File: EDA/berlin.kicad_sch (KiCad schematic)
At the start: 250 parts, among them SW105-? MXSwitch, SW124-? MXSwitch, SW20-? MXSwitch, SW39-? MXSwitch, SW4-? MXSwitch, SW5-? MXSwitch, SW6-? MXSwitch, SW64-? MXSwitch, SW78-? MXSwitch, SW88-? MXSwitch, SW90-? MXSwitch

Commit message: clean up the key matrix
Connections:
- net Col10: now also SW?.1 (Col); no longer SW64-?.1 (Col)
- net Col11: now also SW78-?.1 (Col); no longer SW64-?.1 (Col)
- net Col12: now also SW88-?.1 (Col); no longer SW?.1 (Col)
- net Col13: now also SW90-?.1 (Col); no longer SW78-?.1 (Col)
- net Col14: now also SW?.1 (Col), SW?.1 (Col), SW?.1 (Col), SW?.1 (Col), SW?.1 (Col)
- net Col15: now also SW?.1 (Col), SW?.1 (Col), SW?.1 (Col), SW?.1 (Col), SW?.1 (Col), SW?.1 (Col)
- net Col16: now also SW?.1 (Col), SW?.1 (Col), SW?.1 (Col), SW?.1 (Col), SW?.1 (Col), SW?.S1
- net Col17: now also SW105-?.1 (Col), SW?.1 (Col), SW?.1 (Col), SW?.1 (Col), SW?.1 (Col), SW?.1 (Col)
- net Col18: now also SW124-?.1 (Col), SW?.1 (Col), SW?.1 (Col), SW?.1 (Col), SW?.1 (Col)
- net Col19: now also SW?.1 (Col), SW?.1 (Col), SW?.1 (Col), SW?.1 (Col), SW?.1 (Col), SW?.1 (Col)
- net Col8: now also SW64-?.1 (Col)
- net Col9: now also SW64-?.1 (Col)
- net Row1: now also D?.1 (K), D?.1 (K), D?.1 (K)
- net Row2: now also D?.1 (K), D?.1 (K), D?.1 (K), D?.1 (K), D?.1 (K), D?.1 (K)
- net Row3: now also D?.1 (K), D?.1 (K), D?.1 (K), D?.1 (K), D?.1 (K); no longer D?.1 (K)
- net Row4: now also D?.1 (K), D?.1 (K), D?.1 (K), D?.1 (K), D?.1 (K), D?.1 (K)
- net Row5: now also D?.1 (K), D?.1 (K), D?.1 (K), D?.1 (K), D?.1 (K), D?.1 (K); no longer D?.1 (K)
- net Row6: now also D?.1 (K), D?.1 (K), D?.1 (K), D?.1 (K)
- net Row7: now also D?.1 (K), D?.1 (K), D?.1 (K), D?.1 (K), D?.1 (K), D?.1 (K), D?.1 (K)
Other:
- note added: "#"
- note added: ","
- note added: "<>"
- note added: "Backspace"
- note added: "Backtick"
- note added: "P16"
- note added: "P17"
- note added: "Ä"
- note added: "Ö"
- note added: "Ü"
- note added: "ß"
- note removed: "' ""
- note removed: ", <"
- note removed: "- _"
- note removed: ". >"
- note removed: "/ ?"
- note removed: "; :"
- note removed: "= +"
- note removed: "BackSpace"
- note removed: "ISO Enter"
- note removed: "ISO \ |"
- note removed: "ISO `~{}"
- note removed: "[{"
- note removed: "]}"
- moved on the sheet: D?, L?, SW105-?, SW124-?, SW64-?, SW78-?, SW88-?, SW90-?, SW?

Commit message: blursed schematic
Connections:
- net Col12: now also SW?.1 (Col); no longer SW88-?.1 (Col)
- net Col13: now also SW88-?.1 (Col); no longer SW?.1 (Col)
- net Row4: now also D?.1 (K); no longer D?.1 (K), D?.1 (K)
- net Row5: now also D?.1 (K), D?.1 (K); no longer D?.1 (K), D?.1 (K)
- net Row6: now also D?.1 (K), D?.1 (K), D?.1 (K); no longer D?.1 (K), D?.1 (K)
- net Row7: now also D?.1 (K), D?.1 (K), D?.1 (K); no longer D?.1 (K), D?.1 (K)
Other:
- note added: "' ""
- note added: ", <"
- note added: "- _"
- note added: ". >"
- note added: "/ ?"
- note added: "; :"
- note added: "= +"
- note added: "BackSpace"
- note added: "ISO Enter"
- note added: "ISO \ |"
- note added: "ISO `~{}"
- note added: "[{"
- note added: "]}"
- note added: "back"
- note added: "friday13"
- note added: "play"
- note added: "pmslps4"
- note added: "skip"
- note removed: "#"
- note removed: ","
- note removed: "<>"
- note removed: "Backspace"
- note removed: "Backtick"
- note removed: "P13"
- note removed: "P14"
- note removed: "P15"
- note removed: "P16"
- note removed: "P17"
- note removed: "Ä"
- note removed: "Ö"
- note removed: "Ü"
- note removed: "ß"
- moved on the sheet: D?, L?, SW105-?, SW124-?, SW20-?, SW39-?, SW4-?, SW5-?, SW6-?, SW64-?, SW78-?, SW88-?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

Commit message: added additional schematics
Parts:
- added C? (x16): 10u, Capacitor_SMD:C_1206_3216Metric_Pad1.42x1.75mm_HandSolder, symbol Device:C
- added C? (x16): 100nF, Capacitor_SMD:C_0805_2012Metric_Pad1.15x1.40mm_HandSolder, symbol Device:C
- added C? (x6): 22uF, Capacitor_SMD:C_1206_3216Metric_Pad1.42x1.75mm_HandSolder, symbol Device:C
- added C? (x7): 100n, Capacitor_SMD:C_0805_2012Metric_Pad1.15x1.40mm_HandSolder, symbol Device:C
- added C?: 4.7n, Capacitor_SMD:C_0805_2012Metric_Pad1.15x1.40mm_HandSolder, symbol Device:C
- added D?: RB060M-60TR, acheronComponents:D_SOD-123, symbol Device:D_Schottky_Small
- added D?: 1N4148, acheronComponents:D_SOD-123, symbol Diode:1N4148
- added F?: 1.5A Polyfuse, Fuse:Fuse_1812_4532Metric_Pad1.30x3.40mm_HandSolder, symbol Device:Polyfuse
- added H?: MountingHole_Pad, MountingHole:MountingHole_3.5mm_Pad_Via, symbol Mechanical:MountingHole_Pad
- added HA? (x4): MountingHole, acheronMountingHoles:ToolingHole_1.152mm_(for_JLCPCB_SMT), symbol Mechanical:MountingHole
- added J?: TYPE-C-31-M12_13, acheronConnectors:TYPE-C-31-M-12, symbol Boston-controller-STM32-rescue:TYPE-C-31-M12_13-Acheron
- added J?: Conn_ARM_JTAG_SWD_10, Connector_PinSocket_2.54mm:PinSocket_2x05_P2.54mm_Vertical, symbol acheronSymbols:Conn_ARM_JTAG_SWD_10
- added L? (x2): L_Core_Ferrite, Inductor_SMD:L_0805_2012Metric_Pad1.15x1.40mm_HandSolder, symbol Device:L_Core_Ferrite
- added L?: 6.8uH, SumidaInductor:Sumida0624CDMCC, symbol Device:L
- added LED? (x143): LED, LED_THT:LED_D3.0mm_Clear, symbol Device:LED
- added LED?: NeoPixel_THT, LED_THT:LED_D5.0mm-4_RGB, symbol LED:NeoPixel_THT
- added LOGO?: Logo_Open_Hardware_Large, Symbol:OSHW-Logo_11.4x12mm_SilkScreen, symbol Graphic:Logo_Open_Hardware_Large
- added Q?: DTC123J, Package_TO_SOT_SMD:SOT-23, symbol Transistor_BJT:DTC123J
- added Q?: AO4406AL, acheronComponents:SOIC-8, symbol Boston-controller-STM32-rescue:AO4406AL-Acheron
- added R? (x136): 100 1%, Resistor_SMD:R_0805_2012Metric_Pad1.15x1.40mm_HandSolder, symbol Device:R
- added R? (x2): 5.1k, Resistor_SMD:R_0805_2012Metric_Pad1.15x1.40mm_HandSolder, symbol Device:R
- added R?: 100k, Resistor_SMD:R_0805_2012Metric_Pad1.15x1.40mm_HandSolder, symbol Device:R
- added R? (x3): 330, Resistor_THT:R_Axial_DIN0207_L6.3mm_D2.5mm_P7.62mm_Horizontal, symbol Device:R
- added R?: 1M 1%, Resistor_SMD:R_0805_2012Metric_Pad1.15x1.40mm_HandSolder, symbol Device:R
- added R?: 330k 1%, Resistor_SMD:R_0805_2012Metric_Pad1.15x1.40mm_HandSolder, symbol Device:R
- added R? (x3): 10k, Resistor_SMD:R_0805_2012Metric_Pad1.15x1.40mm_HandSolder, symbol Device:R
- added SW?: SW_Push, Button_Switch_THT:SW_PUSH_6mm_H5mm, symbol Switch:SW_Push
- added U?: SN74LVC1T45DCK, Package_TO_SOT_SMD:SOT-23-6_Handsoldering, symbol Logic_LevelTranslator:SN74LVC1T45DCK
- added U?: STM32F072CBTx, Package_QFP:LQFP-48_7x7mm_P0.5mm, symbol MCU_ST_STM32F0:STM32F072CBTx
- added U?: USBLC6-2SC6, Package_TO_SOT_SMD:SOT-23-6, symbol Power_Protection:USBLC6-2SC6
- added U?: AP63203WU-7, Package_TO_SOT_SMD:TSOT-23-6_HandSoldering, symbol Boston-controller-STM32-rescue:AP63203WU-7-Acheron
- added UA?: STM32F072CBUx, Package_DFN_QFN:QFN-48-1EP_7x7mm_P0.5mm_EP5.6x5.6mm, symbol MCU_ST_STM32F0:STM32F072CBUx
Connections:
- net Col1: now also U?.21 (PB10), UA?.21 (PB10)
- net Col10: now also U?.38 (PA15), UA?.38 (PA15)
- net Col11: now also U?.39 (PB3), UA?.39 (PB3)
- net Col12: now also U?.40 (PB4), UA?.40 (PB4)
- net Col13: now also U?.43 (PB7), UA?.43 (PB7)
- net Col14: now also U?.45 (PB8), UA?.45 (PB8)
- net Col15: now also U?.46 (PB9), UA?.46 (PB9)
- net Col16: now also U?.3 (PC14), UA?.3 (PC14)
- net Col17: now also U?.4 (PC15), UA?.4 (PC15)
- net Col18: now also U?.5 (PF0), UA?.5 (PF0)
- net Col19: now also U?.13 (PA3), UA?.13 (PA3)
- net Col2: now also U?.22 (PB11), UA?.22 (PB11)
- net Col3: now also U?.25 (PB12), UA?.25 (PB12)
- net Col4: now also U?.26 (PB13), UA?.26 (PB13)
- net Col5: now also U?.27 (PB14), UA?.27 (PB14)
- net Col6: now also U?.28 (PB15), UA?.28 (PB15)
- net Col7: now also U?.29 (PA8), UA?.29 (PA8)
- net Col8: now also U?.30 (PA9), UA?.30 (PA9)
- net Col9: now also U?.31 (PA10), UA?.31 (PA10)
- net EncA: now also R?.1, U?.2 (PC13), UA?.2 (PC13)
- net EncB: now also R?.1, U?.6 (PF1), UA?.6 (PF1)
- net GND: now also C?.2, C?.2, C?.2, C?.2, C?.2, C?.2, C?.2, C?.2, C?.2, C?.2, C?.2, C?.2, C?.2, C?.2, C?.2, C?.2, C?.2, D?.2 (A), J?.3 (GND), J?.5 (GND), J?.9 (GNDDetect), J?.A1 (GND), J?.B1 (GND), L?.1, L?.2, LED?.1 (K), LED?.1 (K), LED?.1 (K), LED?.2 (GND), Q?.1, Q?.2, Q?.2 (E), Q?.3, R?.1, R?.1, R?.1, R?.1, R?.1, U?.2 (GND), U?.2 (GND), U?.23 (VSS), U?.35 (VSS), U?.4 (GND), U?.47 (VSS), U?.8 (VSSA), UA?.23 (VSS), UA?.35 (VSS), UA?.47 (VSS), UA?.49 (VSS), UA?.8 (VSSA)
- net Row1: now also U?.41 (PB5), UA?.41 (PB5)
- net Row2: now also U?.42 (PB6), UA?.42 (PB6)
- net Row3: now also U?.17 (PA7), UA?.17 (PA7)
- net Row4: now also U?.18 (PB0), UA?.18 (PB0)
- net Row5: now also U?.19 (PB1), UA?.19 (PB1)
- net Row6: now also U?.20 (PB2), UA?.20 (PB2)
- net Row7: now also U?.14 (PA4), UA?.14 (PA4)
- new net: LED?.2 (A), R?.2 (x127)
- new net: LED?.2 (A), LED?.2 (A), LED?.2 (A), R?.2
- new net: LED?.2 (A), LED?.2 (A), R?.2 (x5)
- new net: R?.2, U?.4 (B)
- new net: J?.A5 (CC1), R?.2
- new net: J?.B5 (CC2), R?.2
- new net: J?.S (SHIELD), L?.1
- new net: R?.2, U?.12 (PA2), UA?.12 (PA2)
- new net: R?.2, U?.11 (PA1), UA?.11 (PA1)
- new net: R?.2, U?.10 (PA0), UA?.10 (PA0)
- new net: D?.1 (K), R?.2
- new net: D?.2 (A), Q?.1 (B), SW?.2
- new net: H?.1, L?.2
- new net: C?.2, L?.1, U?.5 (SW)
- new net: C?.1, U?.6 (BST)
- new net: Q?.4 (G), R?.2, R?.2
- new net: Q?.3 (C), R?.2
- new net +3V3: C?.1, C?.1, C?.1, C?.1, C?.1, C?.1, C?.1, C?.1, C?.1, C?.1, C?.1, C?.1, C?.1, C?.1, C?.1, C?.1, C?.1, C?.1, C?.1, C?.1, C?.1, C?.1, C?.1, C?.1, C?.1, C?.1, C?.1, C?.1, C?.1, C?.1, C?.1, C?.1, C?.1, C?.1, C?.1, C?.1, C?.1, C?.1, C?.1, J?.1 (VCC), L?.2, R?.1, R?.1, R?.1, R?.1, R?.1, R?.1, R?.1, R?.1, R?.1, R?.1, R?.1, R?.1, R?.1, R?.1, R?.1, R?.1, R?.1, R?.1, R?.1, R?.1, R?.1, R?.1, R?.1, R?.1, R?.1, R?.1, R?.1, R?.1, R?.1, R?.1, R?.1, R?.1, R?.1, R?.1, R?.1, R?.1, R?.1, R?.1, R?.1, R?.1, R?.1, R?.1, R?.1, R?.1, R?.1, R?.1, R?.1, R?.1, R?.1, R?.1, R?.1, R?.1, R?.1, R?.1, R?.1, R?.1, R?.1, R?.1, R?.1, R?.1, R?.1, R?.1, R?.1, R?.1, R?.1, R?.1, R?.1, R?.1, R?.1, R?.1, R?.1, R?.1, R?.1, R?.1, R?.1, R?.1, R?.1, R?.1, R?.1, R?.1, R?.1, R?.1, R?.1, R?.1, R?.1, R?.1, R?.1, R?.1, R?.1, R?.1, R?.1, R?.1, R?.1, R?.1, R?.1, R?.1, R?.1, R?.1, R?.1, R?.1, R?.1, R?.1, R?.1, R?.1, R?.1, R?.1, R?.1, R?.1, R?.1, R?.1, R?.1, R?.1, R?.1, R?.1, R?.1, R?.1, R?.1, R?.1, R?.1, R?.1, R?.1, R?.1, R?.1, R?.1, R?.1, R?.1, R?.1, R?.1, R?.1, R?.1, R?.1, R?.1, R?.1, R?.2, R?.2, SW?.1, U?.1 (FB), U?.1 (VBAT), U?.1 (VCCA), U?.24 (VDD), U?.36 (VDDIO2), U?.48 (VDD), U?.5 (DIR), U?.9 (VDDA), UA?.1 (VBAT), UA?.24 (VDD), UA?.36 (VDDIO2), UA?.48 (VDD), UA?.9 (VDDA)
- new net +5V: C?.1, C?.1, C?.1, D?.1 (K), F?.1, LED?.3 (VDD), R?.2, U?.2 (ENABLE), U?.3 (VIN), U?.6 (VCCB)
- new net BOOT0: C?.1, R?.1, R?.2, U?.44 (BOOT0), UA?.44 (BOOT0)
- new net CAP_INDICATOR: LED?.2 (A), R?.1
- new net D+: U?.33 (PA12), U?.4 (I/O2), UA?.33 (PA12)
- new net D-: U?.32 (PA11), U?.6 (I/O1), UA?.32 (PA11)
- new net DI: LED?.4 (DIN), R?.1
- new net Dbus+: J?.A6 (D+), J?.B6 (D+), U?.3 (I/O2)
- new net Dbus-: J?.A7 (D-), J?.B7 (D-), U?.1 (I/O1)
- new net LED_PWM: R?.1, U?.16 (PA6), UA?.16 (PA6)
- new net LED_switch: C?.2, C?.2, C?.2, C?.2, C?.2, C?.2, C?.2, C?.2, C?.2, C?.2, C?.2, C?.2, C?.2, C?.2, C?.2, C?.2, C?.2, C?.2, C?.2, C?.2, C?.2, C?.2, C?.2, C?.2, C?.2, C?.2, C?.2, C?.2, LED?.1 (K), LED?.1 (K), LED?.1 (K), LED?.1 (K), LED?.1 (K), LED?.1 (K), LED?.1 (K), LED?.1 (K), LED?.1 (K), LED?.1 (K), LED?.1 (K), LED?.1 (K), LED?.1 (K), LED?.1 (K), LED?.1 (K), LED?.1 (K), LED?.1 (K), LED?.1 (K), LED?.1 (K), LED?.1 (K), LED?.1 (K), LED?.1 (K), LED?.1 (K), LED?.1 (K), LED?.1 (K), LED?.1 (K), LED?.1 (K), LED?.1 (K), LED?.1 (K), LED?.1 (K), LED?.1 (K), LED?.1 (K), LED?.1 (K), LED?.1 (K), LED?.1 (K), LED?.1 (K), LED?.1 (K), LED?.1 (K), LED?.1 (K), LED?.1 (K), LED?.1 (K), LED?.1 (K), LED?.1 (K), LED?.1 (K), LED?.1 (K), LED?.1 (K), LED?.1 (K), LED?.1 (K), LED?.1 (K), LED?.1 (K), LED?.1 (K), LED?.1 (K), LED?.1 (K), LED?.1 (K), LED?.1 (K), LED?.1 (K), LED?.1 (K), LED?.1 (K), LED?.1 (K), LED?.1 (K), LED?.1 (K), LED?.1 (K), LED?.1 (K), LED?.1 (K), LED?.1 (K), LED?.1 (K), LED?.1 (K), LED?.1 (K), LED?.1 (K), LED?.1 (K), LED?.1 (K), LED?.1 (K), LED?.1 (K), LED?.1 (K), LED?.1 (K), LED?.1 (K), LED?.1 (K), LED?.1 (K), LED?.1 (K), LED?.1 (K), LED?.1 (K), LED?.1 (K), LED?.1 (K), LED?.1 (K), LED?.1 (K), LED?.1 (K), LED?.1 (K), LED?.1 (K), LED?.1 (K), LED?.1 (K), LED?.1 (K), LED?.1 (K), LED?.1 (K), LED?.1 (K), LED?.1 (K), LED?.1 (K), LED?.1 (K), LED?.1 (K), LED?.1 (K), LED?.1 (K), LED?.1 (K), LED?.1 (K), LED?.1 (K), LED?.1 (K), LED?.1 (K), LED?.1 (K), LED?.1 (K), LED?.1 (K), LED?.1 (K), LED?.1 (K), LED?.1 (K), LED?.1 (K), LED?.1 (K), LED?.1 (K), LED?.1 (K), LED?.1 (K), LED?.1 (K), LED?.1 (K), LED?.1 (K), LED?.1 (K), LED?.1 (K), LED?.1 (K), LED?.1 (K), LED?.1 (K), LED?.1 (K), LED?.1 (K), LED?.1 (K), LED?.1 (K), LED?.1 (K), LED?.1 (K), LED?.1 (K), LED?.1 (K), LED?.1 (K), LED?.1 (K), LED?.1 (K), LED?.1 (K), LED?.1 (K), LED?.1 (K), LED?.1 (K), LED?.1 (K), Q?.5 (D), Q?.6, Q?.7, Q?.8
- new net NRST: C?.1, J?.10 (~{RESET}), R?.1, U?.7 (NRST), UA?.7 (NRST)
- new net NUM_INDICATOR: LED?.2 (A), R?.1
- new net RGBLED: U?.15 (PA5), U?.3 (A), UA?.15 (PA5)
- new net SCRL_INDICATOR: LED?.2 (A), R?.1
- new net SWCLK: J?.4 (SWDCLK/TCK), U?.37 (PA14), UA?.37 (PA14)
- new net SWDIO: J?.2 (SWDIO/TMS), U?.34 (PA13), UA?.34 (PA13)
- new net VBUS: C?.1, F?.2, J?.A4 (VBUS), J?.B4 (VBUS), U?.5 (VBUS)
- no-connect marks 0 -> 4
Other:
- note added: "3.3V power"
- note added: "5mm through hole LED (3D-printed version only)"
- note added: "Backlight LEDs"
- note added: "Bulk caps"
- note added: "Bypass cap for the level shifter"
- note added: "Hole for grounding alu case"
- note added: "Holes for JLCPCB SMT tooling"
- note added: "ISP header"
- note added: "LED PWM MOSFET"
- note added: "LQFP-48"
- note added: "Level shifter"
- note added: "Lock LEDs"
- note added: "Logos, holes, misc."
- note added: "Microcontroller"
- note added: "Microprocessor Bypass caps"
- note added: "RGB LED stuff"
- note added: "Reset circuit"
- note added: "SMPS provides more LED current for backlight usage."
- note added: "Sumida 0624CDMCCDS-6R8MC"
- note added: "UFQFPN48 alternate"
- note added: "USB"
- note added: "USB ESD protection"

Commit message: update/fix switch descriptors
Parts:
- gave numbers to parts that had none: 123
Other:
- note added: ","
- note added: "ISO <> |"
- note added: "´"
- note added: "Ä"
- note added: "Ö"
- note added: "Ü"
- note added: "ß"
- note removed: "' ""
- note removed: ", <"
- note removed: "- _"
- note removed: ". >"
- note removed: "/ ?"
- note removed: "; :"
- note removed: "= +"
- note removed: "ISO \ |"
- note removed: "[{"
- note removed: "]}"

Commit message: tset
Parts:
- added R? (x3): 330, Resistor_THT:R_Axial_DIN0207_L6.3mm_D2.5mm_P7.62mm_Horizontal, symbol Device:R
- added R? (x2): 10k, Resistor_SMD:R_0805_2012Metric_Pad1.15x1.40mm_HandSolder, symbol Device:R
- added U?: STM32F072CBTx, Package_QFP:LQFP-48_7x7mm_P0.5mm, symbol MCU_ST_STM32F0:STM32F072CBTx
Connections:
- net +3V3: now also R?.2, R?.2, U?.1 (VBAT), U?.24 (VDD), U?.36 (VDDIO2), U?.48 (VDD), U?.9 (VDDA)
- net BOOT0: now also U?.44 (BOOT0)
- net CAP_INDICATOR: now also R?.1
- net Col1: now also U?.21 (PB10)
- net Col10: now also U?.38 (PA15)
- net Col11: now also U?.39 (PB3)
- net Col12: now also U?.40 (PB4)
- net Col13: now also U?.43 (PB7)
- net Col14: now also U?.45 (PB8)
- net Col15: now also U?.46 (PB9)
- net Col16: now also U?.3 (PC14)
- net Col17: now also U?.4 (PC15)
- net Col18: now also U?.5 (PF0)
- net Col19: now also U?.13 (PA3)
- net Col2: now also U?.22 (PB11)
- net Col3: now also U?.25 (PB12)
- net Col4: now also U?.26 (PB13)
- net Col5: now also U?.27 (PB14)
- net Col6: now also U?.28 (PB15)
- net Col7: now also U?.29 (PA8)
- net Col8: now also U?.30 (PA9)
- net Col9: now also U?.31 (PA10)
- net D+: now also U?.33 (PA12)
- net D-: now also U?.32 (PA11)
- net EncA: now also R?.1, U?.2 (PC13)
- net EncB: now also R?.1, U?.6 (PF1)
- net GND: now also U?.23 (VSS), U?.35 (VSS), U?.47 (VSS), U?.8 (VSSA)
- net LED_PWM: now also U?.16 (PA6)
- net NRST: now also U?.7 (NRST)
- net NUM_INDICATOR: now also R?.1
- net RGBLED: now also U?.15 (PA5)
- net Row1: now also U?.41 (PB5)
- net Row2: now also U?.42 (PB6)
- net Row3: now also U?.17 (PA7)
- net Row4: now also U?.18 (PB0)
- net Row5: now also U?.19 (PB1)
- net Row6: now also U?.20 (PB2)
- net Row7: now also U?.14 (PA4)
- net SCRL_INDICATOR: now also R?.1
- net SWCLK: now also U?.37 (PA14)
- net SWDIO: now also U?.34 (PA13)
- new net: R?.2, U?.10 (PA0)
- new net: R?.2, U?.12 (PA2)
- new net: R?.2, U?.11 (PA1)

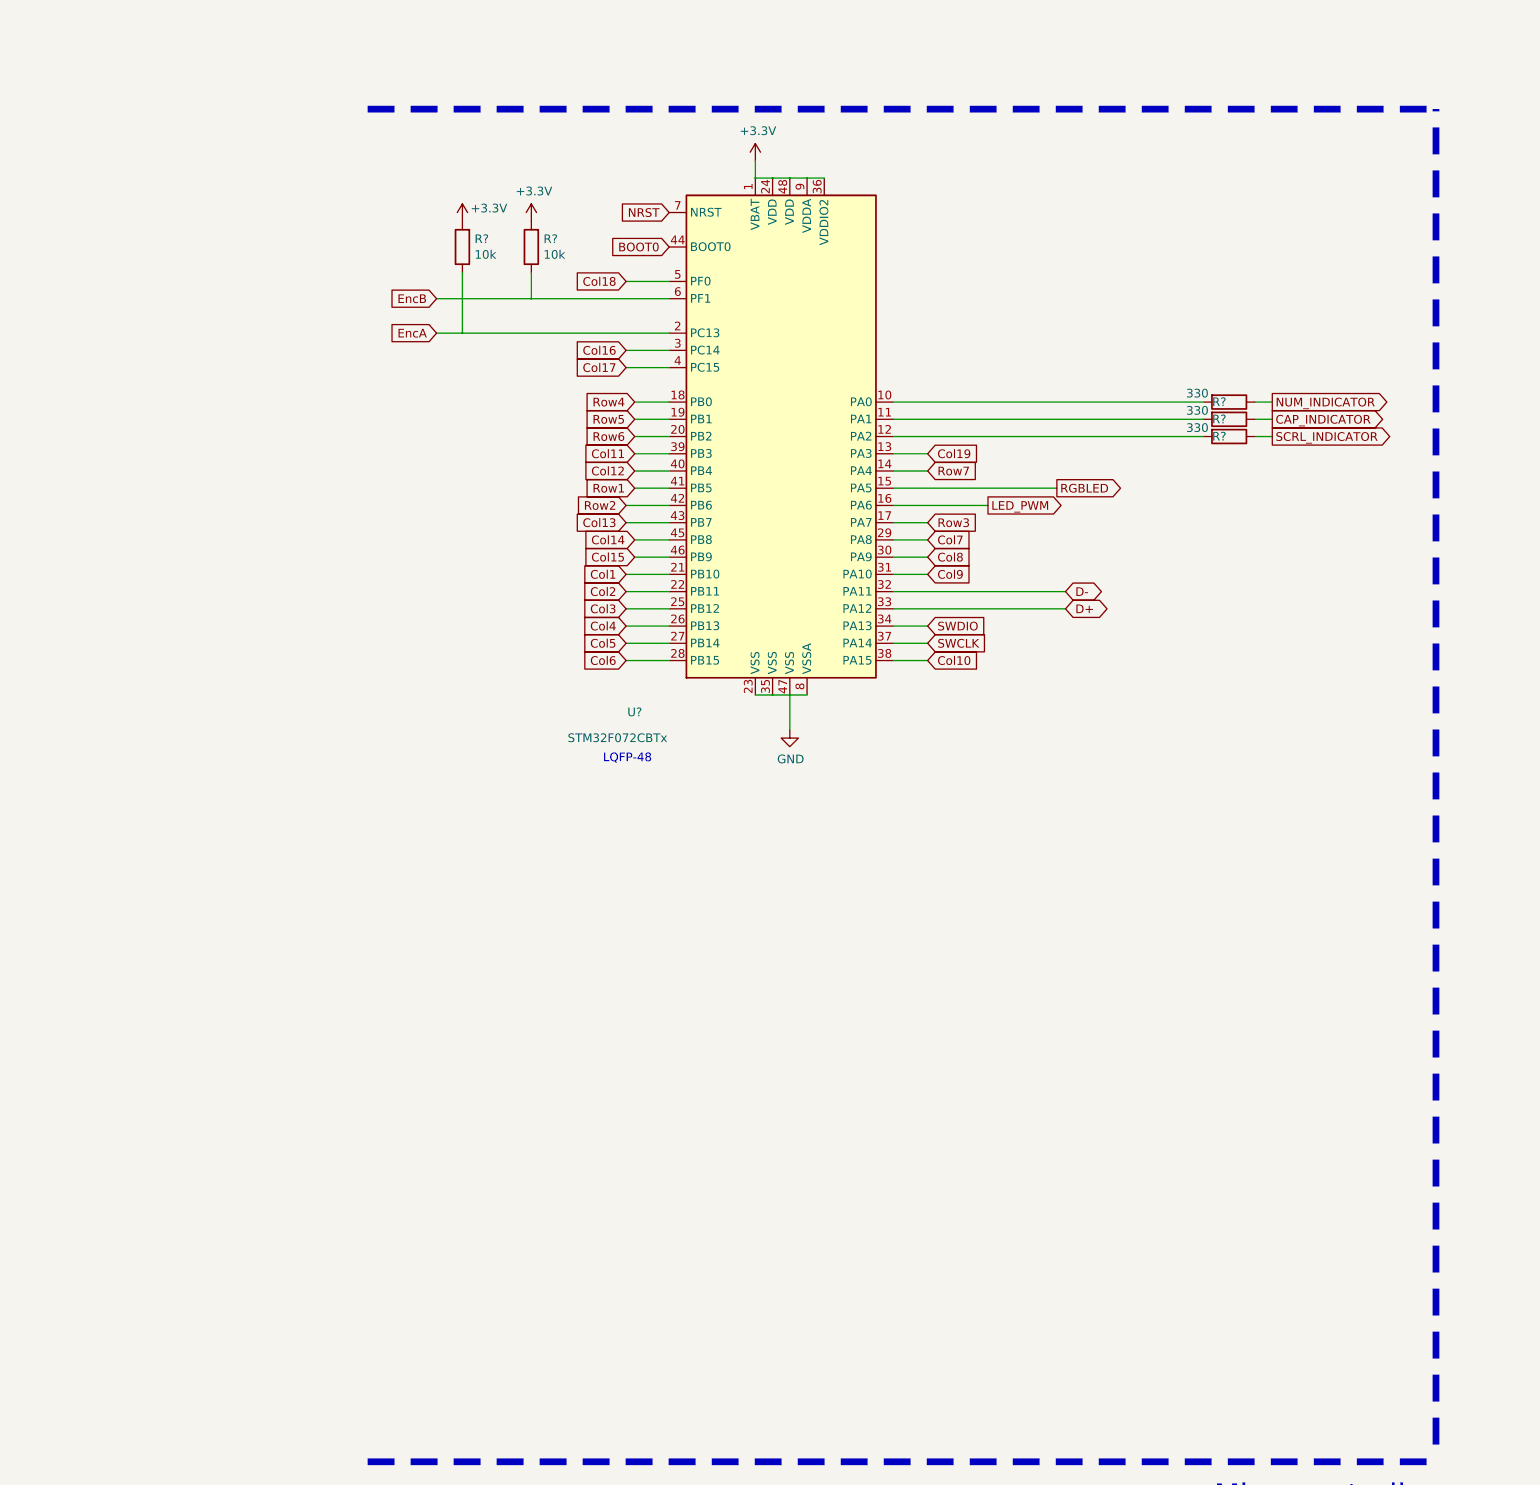
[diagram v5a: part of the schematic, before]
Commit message: added lqfp100 chip
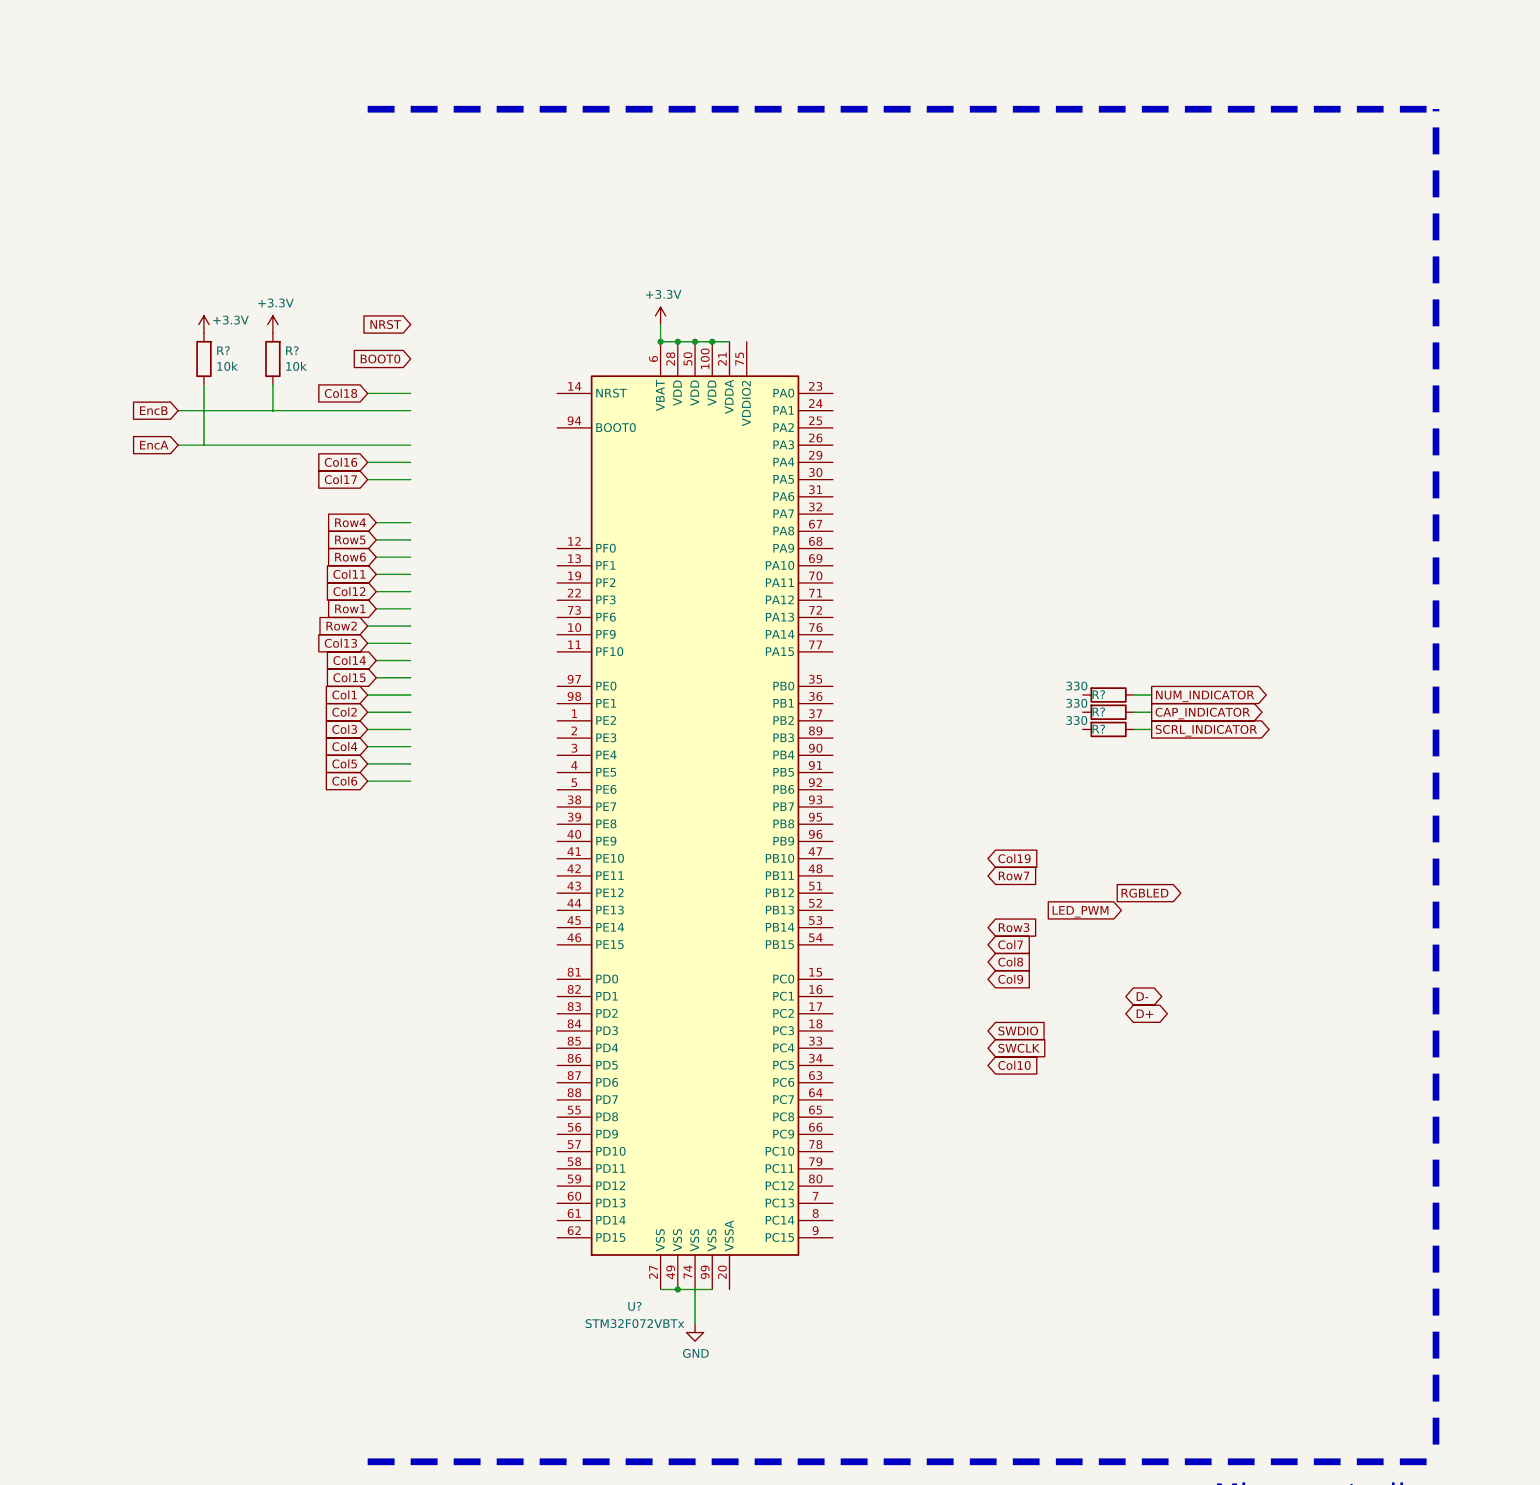
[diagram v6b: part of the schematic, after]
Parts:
- removed U?: STM32F072CBTx, Package_QFP:LQFP-48_7x7mm_P0.5mm, symbol MCU_ST_STM32F0:STM32F072CBTx
- added U?: STM32F072VBTx, Package_QFP:LQFP-100_14x14mm_P0.5mm, symbol MCU_ST_STM32F0:STM32F072VBTx
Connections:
- net +3V3: now also U?.100 (VDD), U?.21 (VDDA), U?.28 (VDD), U?.50 (VDD), U?.6 (VBAT)
- net GND: now also U?.27 (VSS), U?.49 (VSS), U?.74 (VSS), U?.99 (VSS)
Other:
- moved on the sheet: R?
